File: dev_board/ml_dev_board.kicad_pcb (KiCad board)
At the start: 2 copper layers, 100 x 73.2 mm, 56 parts, among them J1 JTAG 3.3V, J2 Canon-Service-Connector, J3 USB_B_Mini, J4 Probe Connector, J5 canon_service_jumper_terminal, Q1 IRLML5203, U1 SN74AUP1T34DCK, U2 SN74AUP1T34DCK, U3 93LCxxBxxOT, U4 LD1117S33TR_SOT223, U5 FT4232H, U6 74HC595, Y1 12MHz

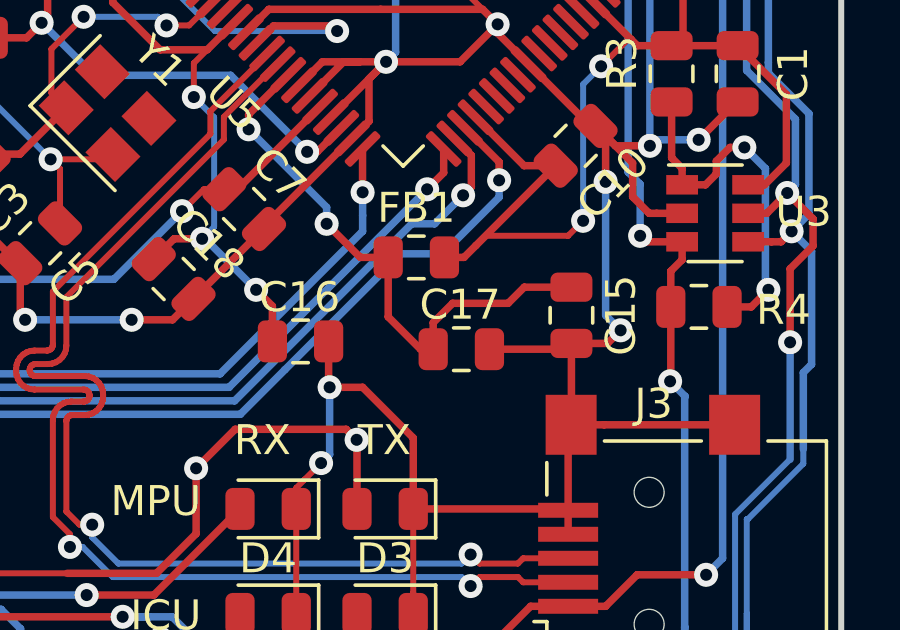
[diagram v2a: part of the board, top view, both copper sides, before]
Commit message: dev_board: use tantalum footprints for polarized caps
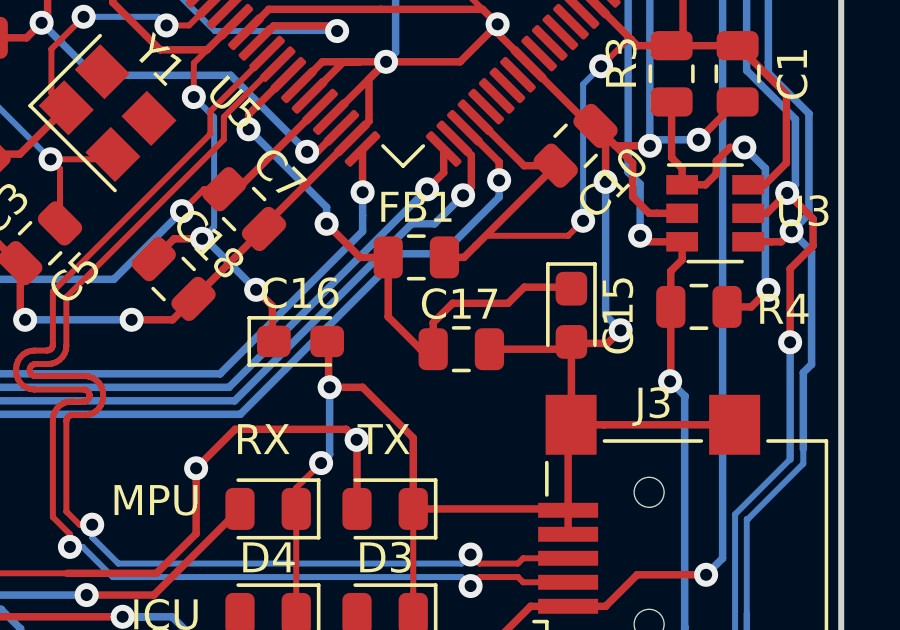
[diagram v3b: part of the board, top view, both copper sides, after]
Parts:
- C15, C16: footprint Capacitor_SMD:C_0805_2012Metric -> Capacitor_Tantalum_SMD:CP_EIA-2012-12_Kemet-R
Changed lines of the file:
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@@
-  )
-  (module Capacitor_SMD:C_0805_2012Metric (layer F.Cu)
-    (at 179.21 101.5 270)
-    (descr "Capacitor SMD 0805 (2012 Metric), square (rectangular) end terminal, IPC_7351 nominal, (Body size source: https://docs.google.com/spreadsheets/d/1BsfQQcO9C6DZCsRaXUlFlo91Tg2WpOkGARC1WS5S8t0/edit?usp=sharing), generated with kicad-footprint-generator")
-    (tags capacitor)
-    (attr smd)
-    (fp_text reference C15 (at 0 -1.65 90) (layer F.SilkS)
-      (effects (font (size 1 1) (thickness 0.15)))
-    )
-    (fp_text value 4.7uF (at 0 1.65 90) (layer F.Fab)
-      (effects (font (size 1 1) (thickness 0.15)))
-    )
-    (fp_line (start 1.68 0.95) (end -1.68 0.95) (layer F.CrtYd) (width 0.05))
-    (fp_line (start 1.68 -0.95) (end 1.68 0.95) (layer F.CrtYd) (width 0.05))
-    (fp_line (start -1.68 -0.95) (end 1.68 -0.95) (layer F.CrtYd) (width 0.05))
-    (fp_line (start -1.68 0.95) (end -1.68 -0.95) (layer F.CrtYd) (width 0.05))
-    (fp_line (start -0.258578 0.71) (end 0.258578 0.71) (layer F.SilkS) (width 0.12))
-    (fp_line (start -0.258578 -0.71) (end 0.258578 -0.71) (layer F.SilkS) (width 0.12))
-    (fp_line (start 1 0.6) (end -1 0.6) (layer F.Fab) (width 0.1))
-    (fp_line (start 1 -0.6) (end 1 0.6) (layer F.Fab) (width 0.1))
-    (fp_line (start -1 -0.6) (end 1 -0.6) (layer F.Fab) (width 0.1))
-    (fp_line (start -1 0.6) (end -1 -0.6) (layer F.Fab) (width 0.1))
-    (fp_text user %R (at 0 0 90) (layer F.Fab)
-      (effects (font (size 0.5 0.5) (thickness 0.08)))
-    )
-    (pad 2 smd roundrect (at 0.9375 0 270) (size 0.975 1.4) (layers F.Cu F.Paste F.Mask) (roundrect_rratio 0.25)
-      (net 2 GND))
-    (pad 1 smd roundrect (at -0.9375 0 270) (size 0.975 1.4) (layers F.Cu F.Paste F.Mask) (roundrect_rratio 0.25)
-      (net 64 "Net-(C15-Pad1)"))
-    (model ${KISYS3DMOD}/Capacitor_SMD.3dshapes/C_0805_2012Metric.wrl
-      (at (xyz 0 0 0))
-      (scale (xyz 1 1 1))
-      (rotate (xyz 0 0 0))
-    )
-  )
-  (module Capacitor_SMD:C_0805_2012Metric (layer F.Cu)
-    (at 170.18 102.37)
-    (descr "Capacitor SMD 0805 (2012 Metric), square (rectangular) end terminal, IPC_7351 nominal, (Body size source: https://docs.google.com/spreadsheets/d/1BsfQQcO9C6DZCsRaXUlFlo91Tg2WpOkGARC1WS5S8t0/edit?usp=sharing), generated with kicad-footprint-generator")
-    (tags capacitor)
-    (attr smd)
-    (fp_text reference C16 (at -0.03 -1.47) (layer F.SilkS)
-      (effects (font (size 1 1) (thickness 0.15)))
-    )
-    (fp_text value 4.7uF (at 0 1.65) (layer F.Fab)
-      (effects (font (size 1 1) (thickness 0.15)))
-    )
-    (fp_line (start -1 0.6) (end -1 -0.6) (layer F.Fab) (width 0.1))
-    (fp_line (start -1 -0.6) (end 1 -0.6) (layer F.Fab) (width 0.1))
-    (fp_line (start 1 -0.6) (end 1 0.6) (layer F.Fab) (width 0.1))
-    (fp_line (start 1 0.6) (end -1 0.6) (layer F.Fab) (width 0.1))
-    (fp_line (start -0.258578 -0.71) (end 0.258578 -0.71) (layer F.SilkS) (width 0.12))
-    (fp_line (start -0.258578 0.71) (end 0.258578 0.71) (layer F.SilkS) (width 0.12))
-    (fp_line (start -1.68 0.95) (end -1.68 -0.95) (layer F.CrtYd) (width 0.05))
-    (fp_line (start -1.68 -0.95) (end 1.68 -0.95) (layer F.CrtYd) (width 0.05))
-    (fp_line (start 1.68 -0.95) (end 1.68 0.95) (layer F.CrtYd) (width 0.05))
-    (fp_line (start 1.68 0.95) (end -1.68 0.95) (layer F.CrtYd) (width 0.05))
-    (fp_text user %R (at 0 0) (layer F.Fab)
-      (effects (font (size 0.5 0.5) (thickness 0.08)))
-    )
-    (pad 1 smd roundrect (at -0.9375 0) (size 0.975 1.4) (layers F.Cu F.Paste F.Mask) (roundrect_rratio 0.25)
-      (net 65 "Net-(C16-Pad1)"))
-    (pad 2 smd roundrect (at 0.9375 0) (size 0.975 1.4) (layers F.Cu F.Paste F.Mask) (roundrect_rratio 0.25)
-      (net 2 GND))
-    (model ${KISYS3DMOD}/Capacitor_SMD.3dshapes/C_0805_2012Metric.wrl
-      (at (xyz 0 0 0))
-      (scale (xyz 1 1 1))
-      (rotate (xyz 0 0 0))
-    )
   )
   (module Capacitor_SMD:C_0805_2012Metric (layer F.Cu)
@@
       (net 76 "Net-(D5-Pad2)"))
     (model ${KISYS3DMOD}/Resistor_SMD.3dshapes/R_0805_2012Metric.wrl
+      (at (xyz 0 0 0))
+      (scale (xyz 1 1 1))
+      (rotate (xyz 0 0 0))
+    )
+  )
+  (module Capacitor_Tantalum_SMD:CP_EIA-2012-12_Kemet-R (layer F.Cu)
+    (at 179.21 101.5 270)
+    (descr "Tantalum Capacitor SMD Kemet-R (2012-12 Metric), IPC_7351 nominal, (Body size from: https://www.vishay.com/docs/40182/tmch.pdf), generated with kicad-footprint-generator")
+    (tags "capacitor tantalum")
+    (attr smd)
+    (fp_text reference C15 (at 0 -1.58 90) (layer F.SilkS)
+      (effects (font (size 1 1) (thickness 0.15)))
+    )
+    (fp_text value 4.7uF (at 0 1.58 90) (layer F.Fab)
+      (effects (font (size 1 1) (thickness 0.15)))
+    )
+    (fp_line (start 1.7 0.88) (end -1.7 0.88) (layer F.CrtYd) (width 0.05))
+    (fp_line (start 1.7 -0.88) (end 1.7 0.88) (layer F.CrtYd) (width 0.05))
+    (fp_line (start -1.7 -0.88) (end 1.7 -0.88) (layer F.CrtYd) (width 0.05))
+    (fp_line (start -1.7 0.88) (end -1.7 -0.88) (layer F.CrtYd) (width 0.05))
+    (fp_line (start -1.71 0.785) (end 1 0.785) (layer F.SilkS) (width 0.12))
+    (fp_line (start -1.71 -0.785) (end -1.71 0.785) (layer F.SilkS) (width 0.12))
+    (fp_line (start 1 -0.785) (end -1.71 -0.785) (layer F.SilkS) (width 0.12))
+    (fp_line (start 1 0.625) (end 1 -0.625) (layer F.Fab) (width 0.1))
+    (fp_line (start -1 0.625) (end 1 0.625) (layer F.Fab) (width 0.1))
+    (fp_line (start -1 -0.3125) (end -1 0.625) (layer F.Fab) (width 0.1))
+    (fp_line (start -0.6875 -0.625) (end -1 -0.3125) (layer F.Fab) (width 0.1))
+    (fp_line (start 1 -0.625) (end -0.6875 -0.625) (layer F.Fab) (width 0.1))
+    (fp_text user %R (at 0 0 90) (layer F.Fab)
+      (effects (font (size 0.5 0.5) (thickness 0.08)))
+    )
+    (pad 1 smd roundrect (at -0.8875 0 270) (size 1.125 1.05) (layers F.Cu F.Paste F.Mask) (roundrect_rratio 0.238095)
+      (net 64 "Net-(C15-Pad1)"))
+    (pad 2 smd roundrect (at 0.8875 0 270) (size 1.125 1.05) (layers F.Cu F.Paste F.Mask) (roundrect_rratio 0.238095)
+      (net 2 GND))
+    (model ${KISYS3DMOD}/Capacitor_Tantalum_SMD.3dshapes/CP_EIA-2012-12_Kemet-R.wrl
+      (at (xyz 0 0 0))
+      (scale (xyz 1 1 1))
+      (rotate (xyz 0 0 0))
+    )
+  )
+  (module Capacitor_Tantalum_SMD:CP_EIA-2012-12_Kemet-R (layer F.Cu)
+    (at 170.18 102.37)
+    (descr "Tantalum Capacitor SMD Kemet-R (2012-12 Metric), IPC_7351 nominal, (Body size from: https://www.vishay.com/docs/40182/tmch.pdf), generated with kicad-footprint-generator")
+    (tags "capacitor tantalum")
+    (attr smd)
+    (fp_text reference C16 (at 0 -1.58) (layer F.SilkS)
+      (effects (font (size 1 1) (thickness 0.15)))
+    )
+    (fp_text value 4.7uF (at 0 1.58) (layer F.Fab)
+      (effects (font (size 1 1) (thickness 0.15)))
+    )
+    (fp_text user %R (at 0 0) (layer F.Fab)
+      (effects (font (size 0.5 0.5) (thickness 0.08)))
+    )
+    (fp_line (start 1 -0.625) (end -0.6875 -0.625) (layer F.Fab) (width 0.1))
+    (fp_line (start -0.6875 -0.625) (end -1 -0.3125) (layer F.Fab) (width 0.1))
+    (fp_line (start -1 -0.3125) (end -1 0.625) (layer F.Fab) (width 0.1))
+    (fp_line (start -1 0.625) (end 1 0.625) (layer F.Fab) (width 0.1))
+    (fp_line (start 1 0.625) (end 1 -0.625) (layer F.Fab) (width 0.1))
+    (fp_line (start 1 -0.785) (end -1.71 -0.785) (layer F.SilkS) (width 0.12))
+    (fp_line (start -1.71 -0.785) (end -1.71 0.785) (layer F.SilkS) (width 0.12))
+    (fp_line (start -1.71 0.785) (end 1 0.785) (layer F.SilkS) (width 0.12))
+    (fp_line (start -1.7 0.88) (end -1.7 -0.88) (layer F.CrtYd) (width 0.05))
+    (fp_line (start -1.7 -0.88) (end 1.7 -0.88) (layer F.CrtYd) (width 0.05))
+    (fp_line (start 1.7 -0.88) (end 1.7 0.88) (layer F.CrtYd) (width 0.05))
+    (fp_line (start 1.7 0.88) (end -1.7 0.88) (layer F.CrtYd) (width 0.05))
+    (pad 2 smd roundrect (at 0.8875 0) (size 1.125 1.05) (layers F.Cu F.Paste F.Mask) (roundrect_rratio 0.238095)
+      (net 2 GND))
+    (pad 1 smd roundrect (at -0.8875 0) (size 1.125 1.05) (layers F.Cu F.Paste F.Mask) (roundrect_rratio 0.238095)
+      (net 65 "Net-(C16-Pad1)"))
+    (model ${KISYS3DMOD}/Capacitor_Tantalum_SMD.3dshapes/CP_EIA-2012-12_Kemet-R.wrl
       (at (xyz 0 0 0))
       (scale (xyz 1 1 1))
@@
     (connect_pads (clearance 0.508))
     (min_thickness 0.254)
-    (fill yes (arc_segments 32) (thermal_gap 0.508) (thermal_bridge_width 0.508))
+    (fill (arc_segments 32) (thermal_gap 0.508) (thermal_bridge_width 0.508))
     (polygon
       (pts
@@
     (connect_pads (clearance 0.508))
     (min_thickness 0.254)
-    (fill yes (arc_segments 32) (thermal_gap 0.508) (thermal_bridge_width 0.508))
+    (fill (arc_segments 32) (thermal_gap 0.508) (thermal_bridge_width 0.508))
     (polygon
       (pts

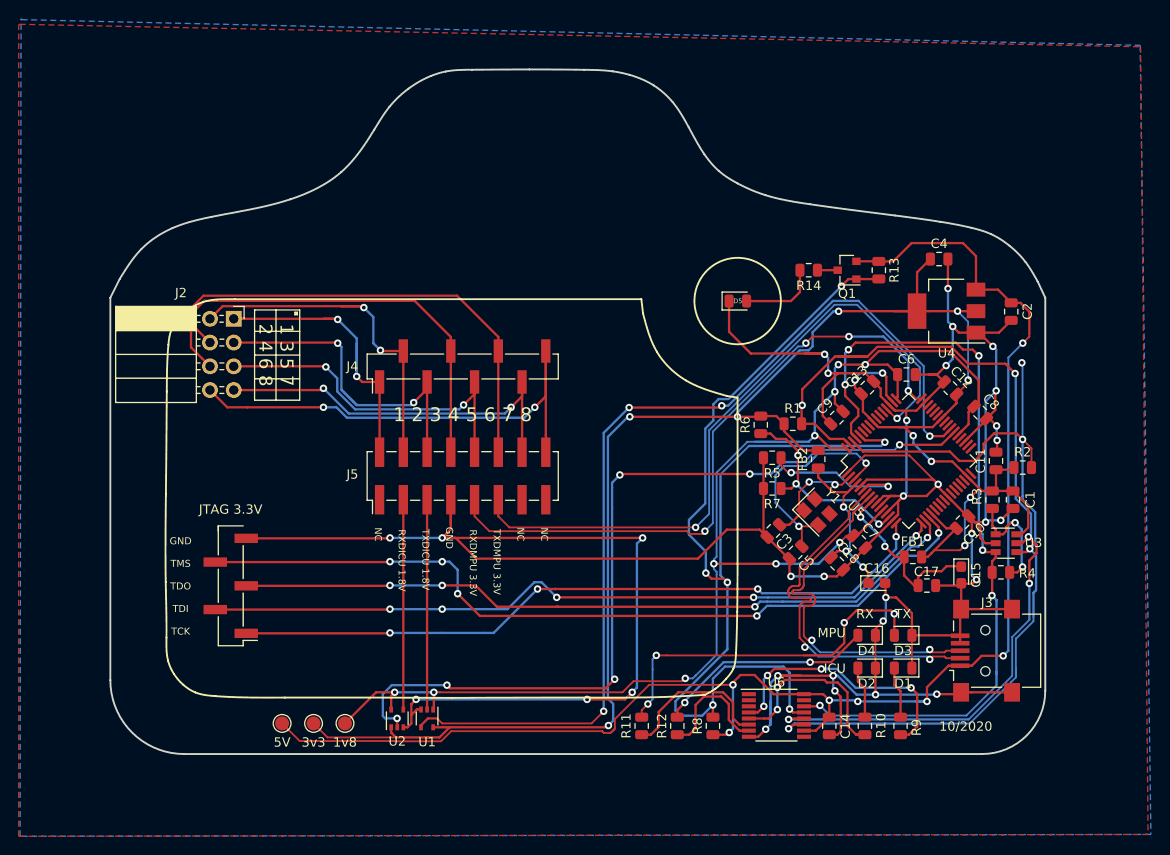
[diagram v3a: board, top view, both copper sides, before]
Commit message: dev_board: fix service connector pinout / use straight connector + cosmetics
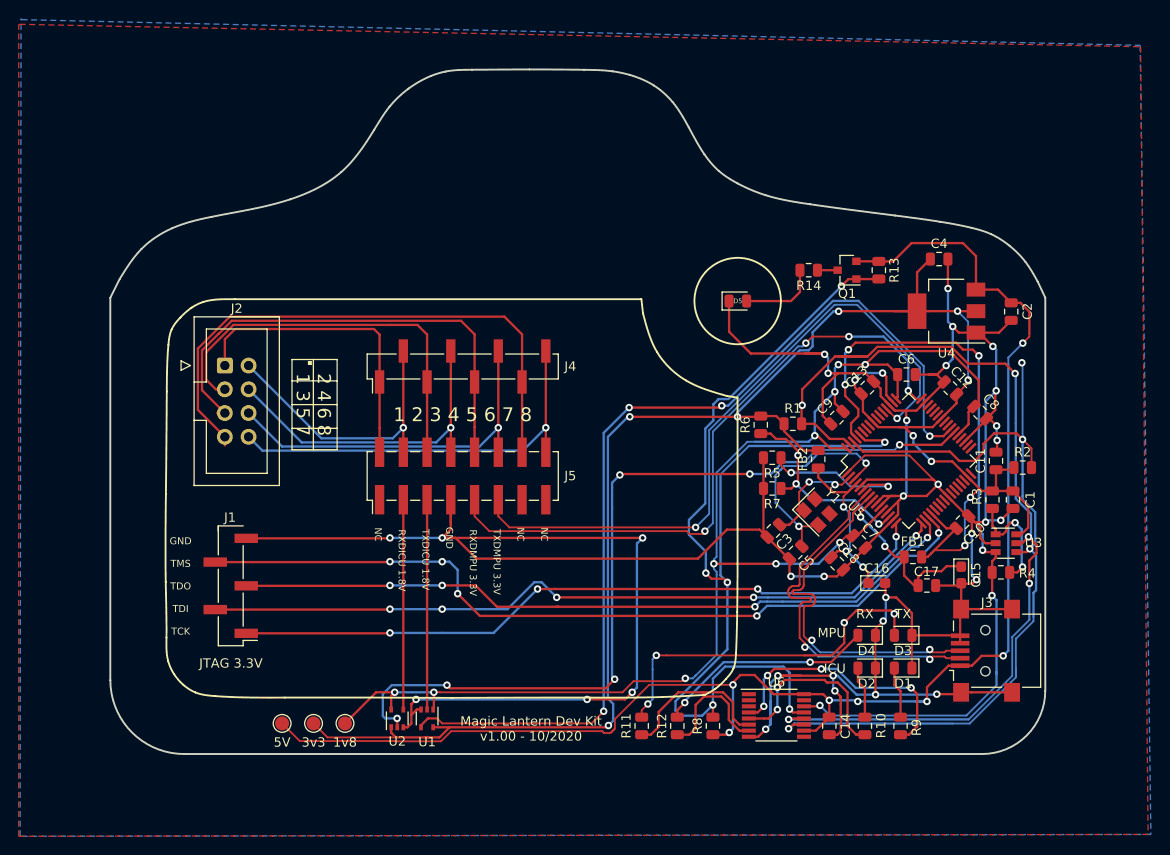
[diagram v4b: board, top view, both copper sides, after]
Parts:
- D1: value Red TXDICU -> Led Red
- D2: value Green RXDICU -> Led Green
- D3: value Red TXDMPU -> Led Red
- D4: value Green RXDMPU -> Led Green
- D5: value Red Status LED -> Led Red
- J2: footprint Connector_PinSocket_2.54mm:PinSocket_2x04_P2.54mm_Horizontal -> Connector_IDC:IDC-Header_2x04_P2.54mm_Vertical
- R13: value 4K7 -> 1K
- moved J2 5.09 mm to (100.5, 79.1)
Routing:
- net /7: track 41.8 -> 61.0 mm, vias 2 -> 0
- net /6: track 54.6 -> 39.9 mm, vias 0 -> 1
- net /5: track 38.0 -> 52.2 mm, vias 2 -> 0
- net /4: track 45.8 -> 35.5 mm, vias 0 -> 1
- net /8: track 53.8 -> 44.2 mm, vias 2 -> 1
- net /2: track 38.2 -> 31.1 mm, vias 2 -> 1
- net /3: track 37.4 -> 43.2 mm, vias 2 -> 0
- net /1: track 34.2 -> 33.4 mm, vias 2 -> 0
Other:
- board text added: "2 4 6 8 1 3 5 7"
- board text added: "Magic Lantern Dev Kit v1.00 - 10/2020"
- board text removed: "1 3 5 7 2 4 6 8"
- board text removed: "10/2020"

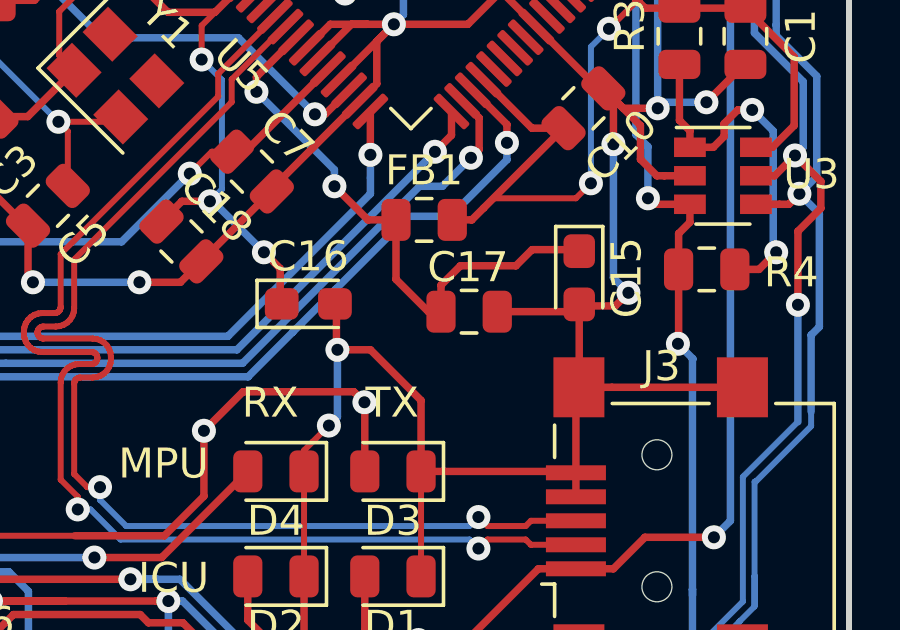
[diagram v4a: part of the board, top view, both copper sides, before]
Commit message: dev_board: use correct footprint for tantalum caps
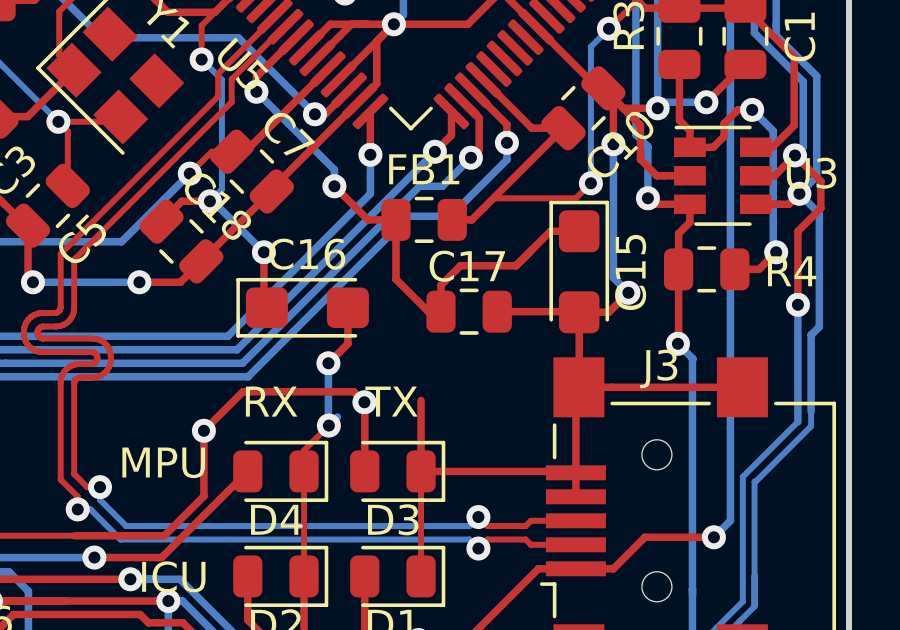
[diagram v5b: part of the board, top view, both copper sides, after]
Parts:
- C15, C16: footprint Capacitor_Tantalum_SMD:CP_EIA-2012-12_Kemet-R -> Capacitor_Tantalum_SMD:CP_EIA-3216-18_Kemet-A
- moved C15 0.20 mm to (179.2, 101.3)
- moved C16 0.13 mm to (170.2, 102.5)
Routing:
- net GND: track 417.0 -> 414.1 mm
- net Net-(C15-Pad1): track 19.0 -> 20.0 mm
- net Net-(C16-Pad1): track 20.7 -> 21.2 mm

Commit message: dev board: fix mini usb symbol
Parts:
- removed G***: LOGO, ml_dev_board:ml_logo
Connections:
- J5 pad 11: Net-(J5-Pad11) -> (no net)
- J5 pad 17: Net-(J5-Pad17) -> (no net)
- J5 pad 18: Net-(J5-Pad18) -> (no net)
- U5 pad 21: Net-(U5-Pad21) -> (no net)
- U5 pad 22: Net-(U5-Pad22) -> (no net)
- U5 pad 23: Net-(U5-Pad23) -> (no net)
- U5 pad 24: Net-(U5-Pad24) -> (no net)
- U5 pad 26: /FTDI/RXFPU -> (no net)
- U5 pad 27: /FTDI/TXFPU -> (no net)
- U5 pad 28: Net-(U5-Pad28) -> (no net)
- U5 pad 29: Net-(U5-Pad29) -> (no net)
- U5 pad 30: Net-(U5-Pad30) -> (no net)
- U5 pad 32: Net-(U5-Pad32) -> (no net)
- U5 pad 33: Net-(U5-Pad33) -> (no net)
- U5 pad 34: Net-(U5-Pad34) -> (no net)
- U5 pad 36: Net-(U5-Pad36) -> (no net)
- U5 pad 40: Net-(U5-Pad40) -> (no net)
- U5 pad 41: Net-(U5-Pad41) -> (no net)
- U5 pad 43: Net-(U5-Pad43) -> (no net)
- U5 pad 44: Net-(U5-Pad44) -> (no net)
- U5 pad 45: Net-(U5-Pad45) -> (no net)
- U5 pad 46: Net-(U5-Pad46) -> (no net)
- U5 pad 53: Net-(U5-Pad53) -> (no net)
- U5 pad 54: Net-(U5-Pad54) -> (no net)
- U5 pad 55: Net-(U5-Pad55) -> (no net)
- U5 pad 57: Net-(U5-Pad57) -> (no net)
- U5 pad 58: Net-(U5-Pad58) -> (no net)
- U5 pad 59: Net-(U5-Pad59) -> (no net)
- U6 pad 1: Net-(U6-Pad1) -> (no net)
- U6 pad 15: Net-(U6-Pad15) -> (no net)
- U6 pad 2: Net-(U6-Pad2) -> (no net)
- U6 pad 3: Net-(U6-Pad3) -> (no net)
- U6 pad 9: Net-(U6-Pad9) -> (no net)
